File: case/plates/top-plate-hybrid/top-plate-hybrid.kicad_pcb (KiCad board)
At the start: 2 copper layers, 103.9 x 80.6 mm, 0 parts

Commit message: Mcu cover (#7)
* more plates

* updated workflow

* mcu cover

* small change
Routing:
- added copper zone on B.Cu, net (none)
- added copper zone on F.Cu, net (none)
- removed copper zone on B.Cu, net GND
- removed copper zone on F.Cu, net GND
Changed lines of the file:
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@@
 	(paper "A4")
 	(title_block
-		(title "hybrid-top-plate")
+		(title "VOID Top Plate Hybrid")
 		(date "2024-11-17")
 		(rev "0.5.9")
@@
 	)
 	(net 0 "")
-	(net 1 "GND")
 	(gr_circle
 		(center 74.609926 64.290043)
@@
 		(stroke
 			(width 0.15)
-			(type default)
+			(type solid)
 		)
 		(fill none)
@@
 	)
 	(zone
-		(net 1)
-		(net_name "GND")
+		(net 0)
+		(net_name "")
 		(layers "F&B.Cu")
 		(hatch edge 0.5)

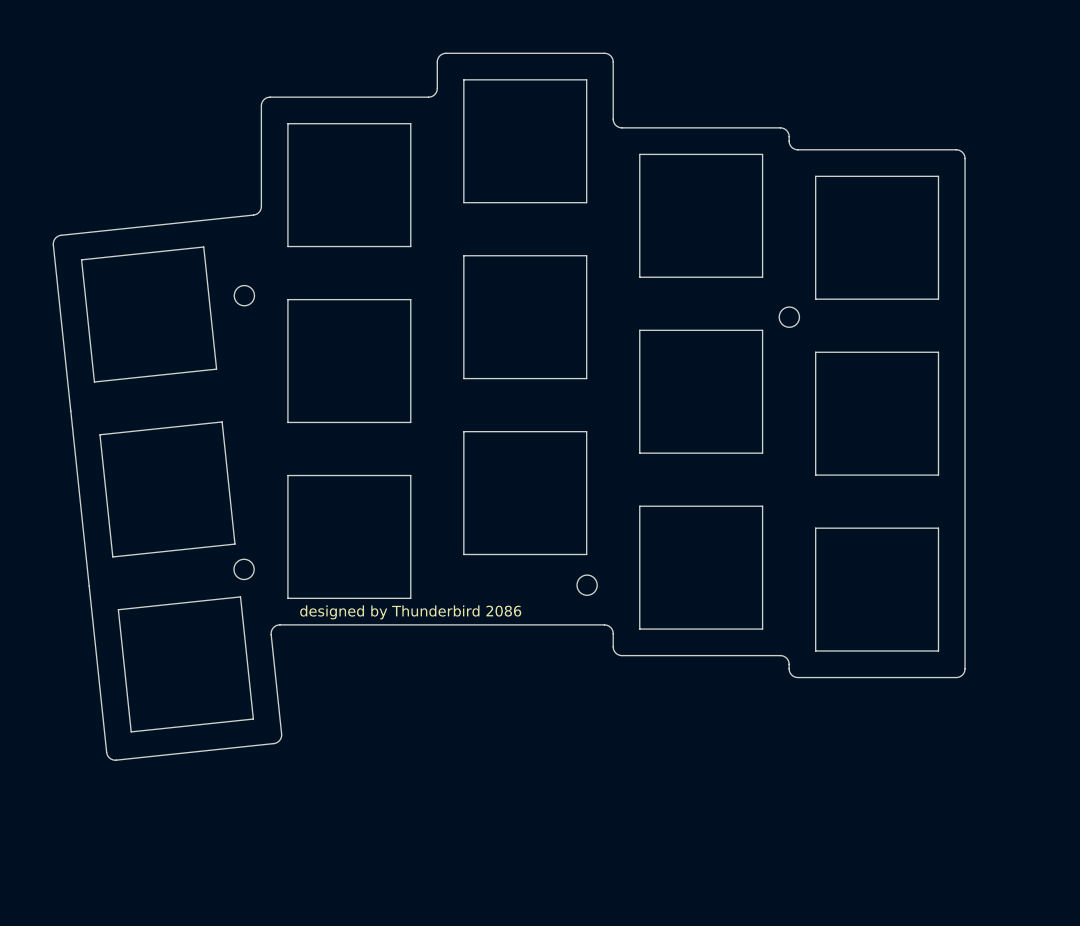
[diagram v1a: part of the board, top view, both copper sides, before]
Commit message: amended hybrid top
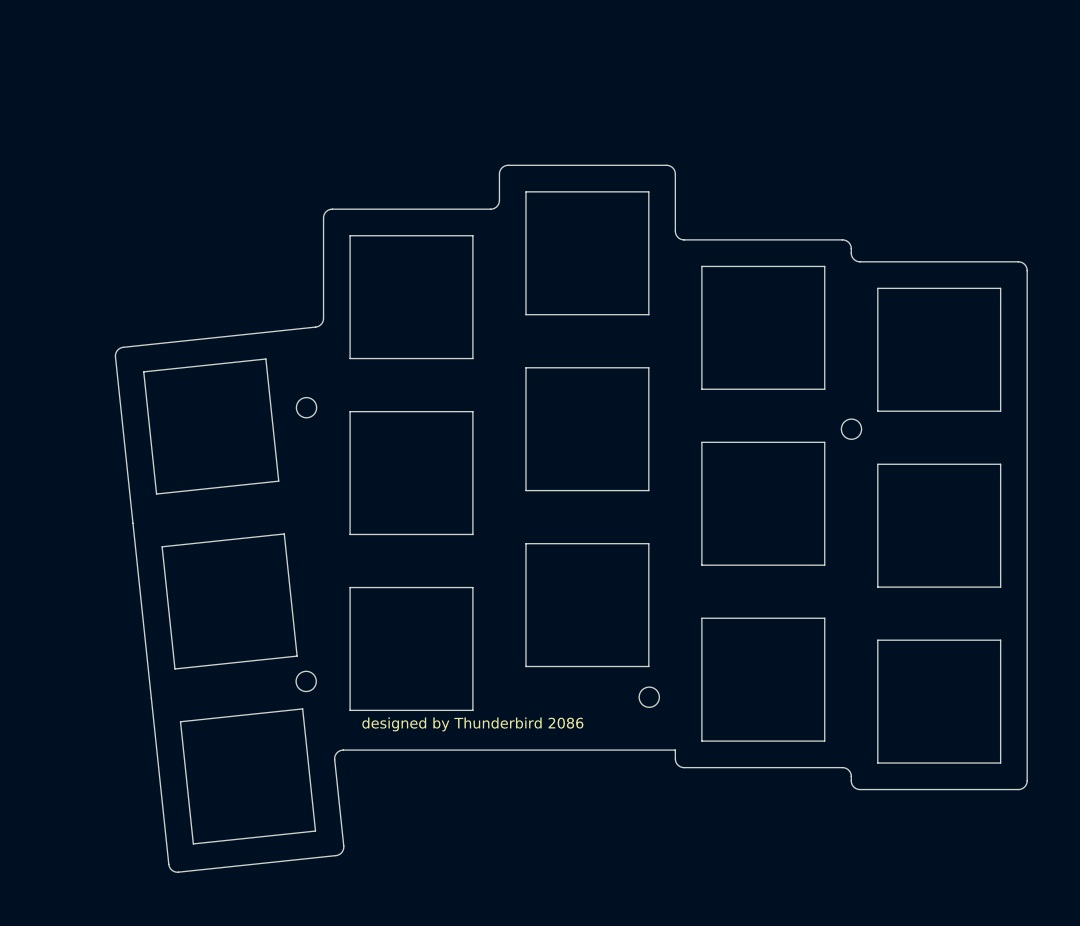
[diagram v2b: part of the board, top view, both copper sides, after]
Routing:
- added copper zone on B.Cu, net GND
- added copper zone on F.Cu, net GND
- removed copper zone on B.Cu, net (none)
- removed copper zone on F.Cu, net (none)
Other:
- outline, holes or cut-outs redrawn

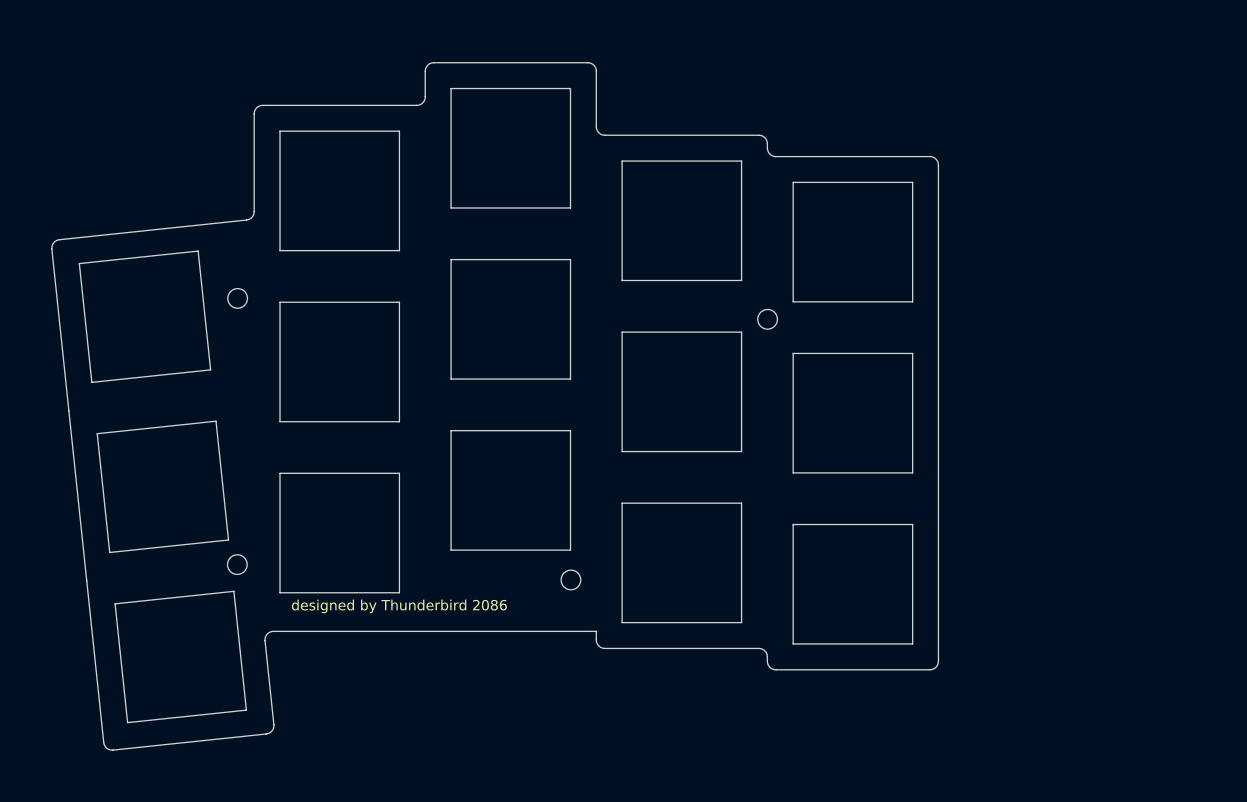
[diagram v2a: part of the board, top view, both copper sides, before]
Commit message: Changed TRRS to USB-C connector (#14)
* usb-c mod for hybrid

* updated
  - submodule
  - ergogen yaml
  - schematic and pcb

* updated cherry-mx

usb-c for communication between left and right hand sides

* updated choc

* updated choc

* fixed corner

* void-choc

* ergogen
  - bottom plate
  - charger plate

* updated choc

* updated ergogen

* cherry-mx
* hybrid-mx

* updated ergogen for VOID Choc

* refreshed submodule

* updated ergogen yaml

* updated PCBs

* updated version
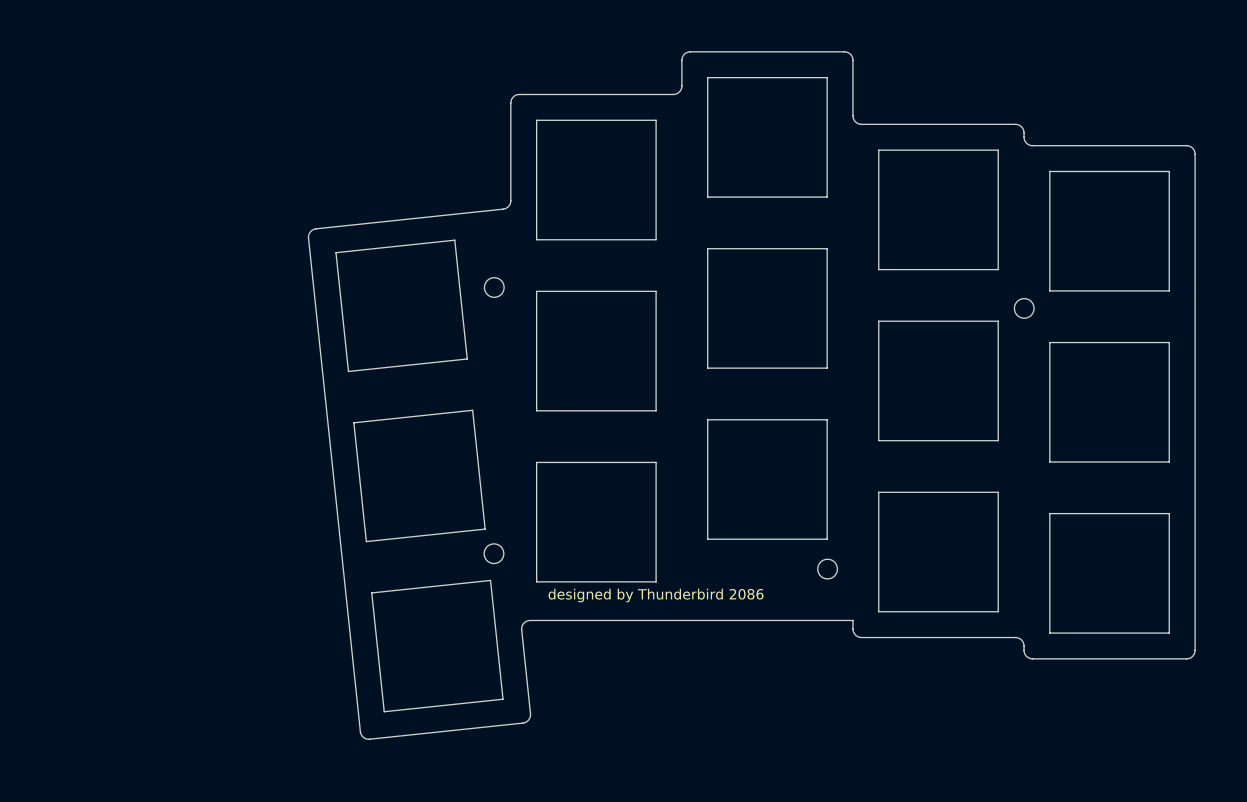
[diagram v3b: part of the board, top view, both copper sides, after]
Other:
- board text added: "offset: 90, 70 from origin"
